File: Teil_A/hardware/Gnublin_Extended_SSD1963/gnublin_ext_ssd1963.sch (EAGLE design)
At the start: 8 parts

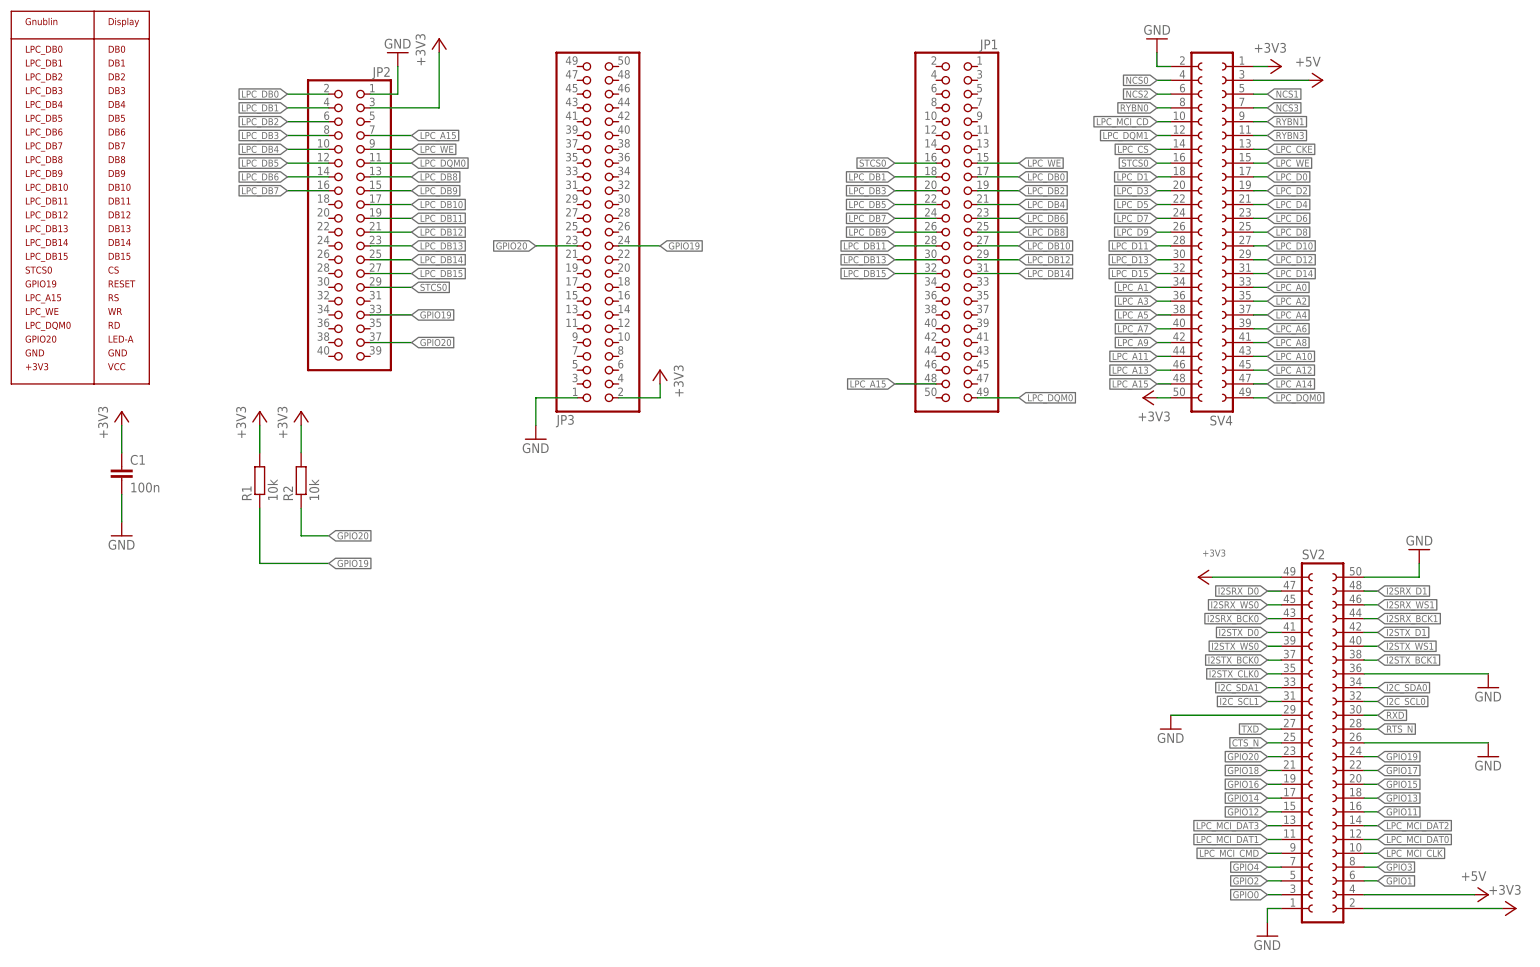
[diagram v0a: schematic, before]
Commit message: updated TEIL_A schematics and layout; git commit -am 'updated TEIL_A schematics and layout
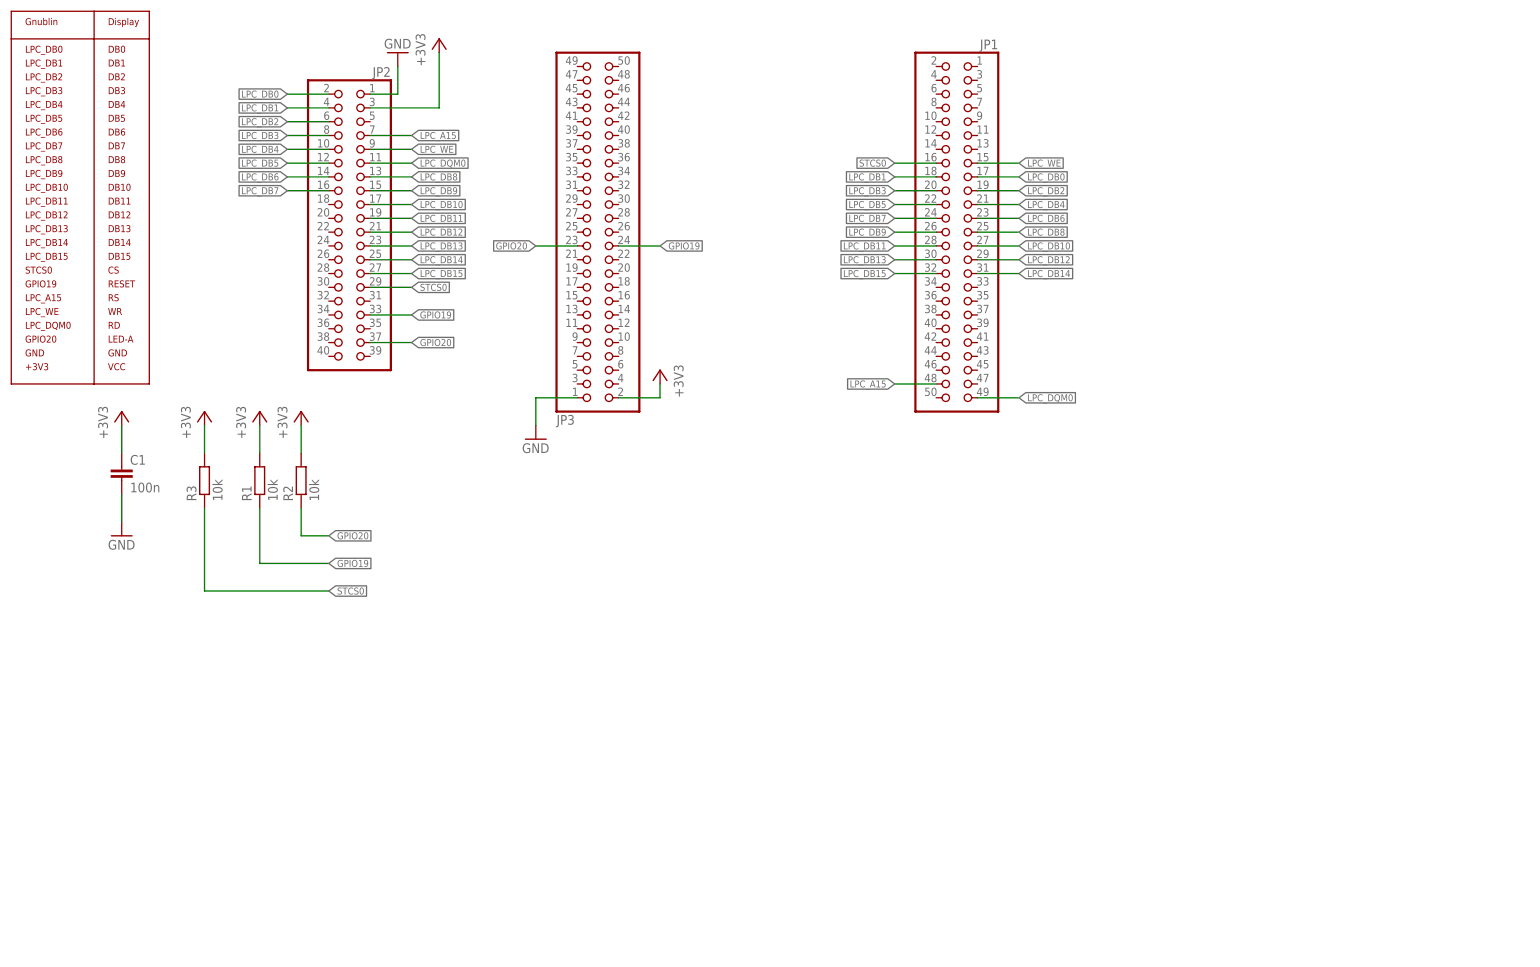
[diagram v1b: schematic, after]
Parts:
- removed SV2, SV4: (no value), con-lsta:FE25-2
- added R3: 10k, rcl:R-EU_R0603
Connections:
- removed net +5V: SV2.4, SV4.3
- removed net CTS_N: SV2.25
- removed net GPIO0: SV2.3
- removed net GPIO1: SV2.6
- removed net GPIO11: SV2.16
- removed net GPIO12: SV2.15
- removed net GPIO13: SV2.18
- removed net GPIO14: SV2.17
- removed net GPIO15: SV2.20
- removed net GPIO16: SV2.19
- removed net GPIO17: SV2.22
- removed net GPIO18: SV2.21
- removed net GPIO2: SV2.5
- removed net GPIO3: SV2.8
- removed net GPIO4: SV2.7
- removed net I2C_SCL0: SV2.32
- removed net I2C_SCL1: SV2.31
- removed net I2C_SDA0: SV2.34
- removed net I2C_SDA1: SV2.33
- removed net I2SRX_BCK0: SV2.43
- removed net I2SRX_BCK1: SV2.44
- removed net I2SRX_D0: SV2.47
- removed net I2SRX_D1: SV2.48
- removed net I2SRX_WS0: SV2.45
- removed net I2SRX_WS1: SV2.46
- removed net I2STX_BCK0: SV2.37
- removed net I2STX_BCK1: SV2.38
- removed net I2STX_CLK0: SV2.35
- removed net I2STX_D0: SV2.41
- removed net I2STX_D1: SV2.42
- removed net I2STX_WS0: SV2.39
- removed net I2STX_WS1: SV2.40
- removed net LPC_A0: SV4.33
- removed net LPC_A1: SV4.34
- removed net LPC_A10: SV4.43
- removed net LPC_A11: SV4.44
- removed net LPC_A12: SV4.45
- removed net LPC_A13: SV4.46
- removed net LPC_A14: SV4.47
- removed net LPC_A2: SV4.35
- removed net LPC_A3: SV4.36
- removed net LPC_A4: SV4.37
- removed net LPC_A5: SV4.38
- removed net LPC_A6: SV4.39
- removed net LPC_A7: SV4.40
- removed net LPC_A8: SV4.41
- removed net LPC_A9: SV4.42
- removed net LPC_CKE: SV4.13
- removed net LPC_CS: SV4.14
- removed net LPC_D0: SV4.17
- removed net LPC_D1: SV4.18
- removed net LPC_D10: SV4.27
- removed net LPC_D11: SV4.28
- removed net LPC_D12: SV4.29
- removed net LPC_D13: SV4.30
- removed net LPC_D14: SV4.31
- removed net LPC_D15: SV4.32
- removed net LPC_D2: SV4.19
- removed net LPC_D3: SV4.20
- removed net LPC_D4: SV4.21
- removed net LPC_D5: SV4.22
- removed net LPC_D6: SV4.23
- removed net LPC_D7: SV4.24
- removed net LPC_D8: SV4.25
- removed net LPC_D9: SV4.26
- removed net LPC_DQM1: SV4.12
- removed net LPC_MCI_CD: SV4.10
- removed net LPC_MCI_CLK: SV2.10
- removed net LPC_MCI_CMD: SV2.9
- removed net LPC_MCI_DAT0: SV2.12
- removed net LPC_MCI_DAT1: SV2.11
- removed net LPC_MCI_DAT2: SV2.14
- removed net LPC_MCI_DAT3: SV2.13
- removed net NCS0: SV4.4
- removed net NCS1: SV4.5
- removed net NCS2: SV4.6
- removed net NCS3: SV4.7
- removed net RTS_N: SV2.28
- removed net RXD: SV2.30
- removed net RYBN0: SV4.8
- removed net RYBN1: SV4.9
- removed net RYBN3: SV4.11
- removed net TXD: SV2.27
- net +3V3: now also R3.2; no longer SV2.2, SV2.49, SV4.1, SV4.50
- net GND: no longer SV2.1, SV2.26, SV2.29, SV2.36, SV2.50, SV4.2
- net GPIO19: no longer SV2.24
- net GPIO20: no longer SV2.23
- net LPC_A15: no longer SV4.48
- net LPC_DQM0: no longer SV4.49
- net LPC_WE: no longer SV4.15
- net STCS0: now also R3.1; no longer SV4.16
